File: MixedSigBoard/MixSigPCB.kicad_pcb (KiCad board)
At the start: 2 copper layers, 108 parts, among them J3 2x5 1.27mm, J4 USB_C_Receptacle_USB2.0, U1 REF3033AIDBZT, U10 HT7533-1, U11 MCP6001T-E/OT, U3 MCP6001T-E/OT, U4 MCP6001T-E/OT, U6 MCP6001T-E/OT, U7 STM32F103CBT6, U8 USBLC6-2SC6, U9 TLV62569DBV, Y1 16MHz

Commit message: -Renumber components to match sheet number -Created PCB Constraints and Set-up
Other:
- copper layers 2 -> 4
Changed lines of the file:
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@@
 	(generator_version "9.0")
 	(general
-		(thickness 1.6)
+		(thickness 1.591)
 		(legacy_teardrops no)
 	)
@@
 	(layers
 		(0 "F.Cu" signal)
+		(4 "In1.Cu" power)
+		(6 "In2.Cu" power)
 		(2 "B.Cu" signal)
 		(9 "F.Adhes" user "F.Adhesive")
@@
 	)
 	(setup
+		(stackup
+			(layer "F.SilkS"
+				(type "Top Silk Screen")
+			)
+			(layer "F.Paste"
+				(type "Top Solder Paste")
+			)
+			(layer "F.Mask"
+				(type "Top Solder Mask")
+				(thickness 0.01)
+			)
+			(layer "F.Cu"
+				(type "copper")
+				(thickness 0.035)
+			)
+			(layer "dielectric 1"
+				(type "prepreg")
+				(thickness 0.2)
+				(material "FR4")
+				(epsilon_r 4.6)
+				(loss_tangent 0.02)
+			)
+			(layer "In1.Cu"
+				(type "copper")
+				(thickness 0.018)
+			)
+			(layer "dielectric 2"
+				(type "core")
+				(thickness 1.065)
+				(material "FR4")
+				(epsilon_r 4.6)
+				(loss_tangent 0.02)
+			)
+			(layer "In2.Cu"
+				(type "copper")
+				(thickness 0.018)
+			)
+			(layer "dielectric 3"
+				(type "prepreg")
+				(thickness 0.2)
+				(material "FR4")
+				(epsilon_r 4.6)
+				(loss_tangent 0.02)
+			)
+			(layer "B.Cu"
+				(type "copper")
+				(thickness 0.035)
+			)
+			(layer "B.Mask"
+				(type "Bottom Solder Mask")
+				(thickness 0.01)
+			)
+			(layer "B.Paste"
+				(type "Bottom Solder Paste")
+			)
+			(layer "B.SilkS"
+				(type "Bottom Silk Screen")
+			)
+			(copper_finish "ENIG")
+			(dielectric_constraints no)
+		)
 		(pad_to_mask_clearance 0)
 		(allow_soldermask_bridges_in_footprints no)

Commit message: Add all footprints
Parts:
- added J1: 031-5640-1010, MixSig_Footprints_KiCad6:AMPHENOL-BNC-031-5640-1010, F.Cu at (191.1, 106.2)
- added J2: 031-5640-1010, MixSig_Footprints_KiCad6:AMPHENOL-BNC-031-5640-1010, F.Cu at (191.1, 124.7)
- added L2: CMF3216F-900-2P-T, MixSig_Footprints_KiCad6:CMC-1206, F.Cu at (207.7, 123.0)
- added L4: 68u, MixSig_Footprints_KiCad6:MWSA0603S, F.Cu at (210.3, 115.5)
- added U2: ADC141S626CIMM_NOPB, MixSig_Footprints_KiCad6:VSSOP-10, F.Cu at (201.3, 96.6)
- added U5: DAC7563SDGSR, MixSig_Footprints_KiCad6:VSSOP-10, F.Cu at (201.3, 115.1)
- renumbered C2 to C1, C11 to C10, C12 to C11, C13 to C12, C14 to C13, C15 to C14, C16 to C15, C17 to C16, C18 to C17, C19 to C18, C20 to C19, C3 to C2, C21 to C20, C22 to C21, C23 to C22, C24 to C23, C25 to C24, C26 to C25, C27 to C26, C28 to C27, C29 to C28, C30 to C29, C4 to C3, C31 to C30, C32 to C31, C33 to C32, C34 to C33, C35 to C34, C36 to C35, C37 to C36, C1 to C37, C45 to C38, C38 to C39, C5 to C4, C39 to C40, C40 to C41, C41 to C42, C42 to C43, C43 to C44, C44 to C45, C6 to C5, C7 to C6, C8 to C7, C9 to C8, C10 to C9, L2 to L1, L1 to L3, R2 to R1, R11 to R10, R12 to R11, R13 to R12, R14 to R13, R15 to R14, R16 to R15, R17 to R16, R18 to R17, R19 to R18, R20 to R19, R3 to R2, R21 to R20, R22 to R21, R23 to R22, R24 to R23, R25 to R24, R26 to R25, R27 to R26, R28 to R27, R29 to R28, R30 to R29, R4 to R3, R31 to R30, R1 to R31, R5 to R4, R6 to R5, R7 to R6, R8 to R7, R9 to R8, R10 to R9

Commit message: add pcb footprints
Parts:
- moved L2 76.8 mm to (141.2, 84.5)
- moved D3 40.0 mm to (171.5, 111.7)
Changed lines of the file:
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@@
 		)
 		(embedded_fonts no)
-		(model "C:/Users/phili/OneDrive/Electrical/STEP FILES/BNC-31-5640-1010.stp"
+		(model "${KICAD9_3DMODEL_DIR}/Connector_USB.3dshapes/31-5640-1010.stp"
 			(offset
 				(xyz 0 30.15 8)
@@
 		)
 		(embedded_fonts no)
-		(model "${KICAD9_3DMODEL_DIR}/Connector_USB.3dshapes/USB_C_Receptacle_HRO_TYPE-C-31-M-12.step"
+		(model "${KICAD9_3DMODEL_DIR}/Connector_USB.3dshapes/HRO_TYPE-C-31-M-12.step"
 			(offset
-				(xyz 0 0 0)
+				(xyz -4.45 -3.9 0)
 			)
 			(scale
@@
 			)
 			(rotate
-				(xyz 0 0 0)
+				(xyz -0 -0 -0)
 			)
 		)
@@
 	(footprint "MixSig_Footprints_KiCad6:CMC-1206"
 		(layer "F.Cu")
-		(at 207.675 122.95)
+		(at 141.175 84.45)
 		(property "Reference" "L2"
 			(at 0 -3 0)
@@
 		)
 		(embedded_fonts no)
-		(model "C:/Users/phili/OneDrive/Electrical/STEP FILES/CMC-1206.step"
+		(model "${KICAD9_3DMODEL_DIR}/LED_SMD.3dshapes/Coilcraft-1206CS.step"
 			(offset
 				(xyz 0 0 0)
@@
 		)
 		(embedded_fonts no)
-		(model "C:/Users/phili/OneDrive/Electrical/STEP FILES/MWSA0603S.STEP"
+		(model "${KICAD9_3DMODEL_DIR}/Connector_USB.3dshapes/IND_MWSA0603S_SNL.step"
 			(offset
 				(xyz 0 0 0)
@@
 	(footprint "LED_SMD:LED_Avago_PLCC4_3.2x2.8mm_CW"
 		(layer "F.Cu")
-		(at 131.57 114.31)
+		(at 171.5 111.695)
 		(descr "3.2mm x 2.8mm PLCC4 RGB LED, https://docs.broadcom.com/docs/AV02-4186EN")
 		(tags "LED Avago PLCC-4 3528 ASMB-MTB0-0A3A2")
@@
 		)
 		(embedded_fonts no)
-		(model "${KICAD9_3DMODEL_DIR}/LED_SMD.3dshapes/LED_Avago_PLCC4_3.2x2.8mm_CW.step"
+		(model "${KICAD9_3DMODEL_DIR}/LED_SMD.3dshapes/PLCC4.stp"
 			(offset
 				(xyz 0 0 0)
@@
 		)
 		(embedded_fonts no)
-		(model "C:/Users/phili/OneDrive/Electrical/STEP FILES/BNC-31-5640-1010.stp"
+		(model "${KICAD9_3DMODEL_DIR}/Connector_USB.3dshapes/31-5640-1010.stp"
 			(offset
 				(xyz 0 30.15 8)

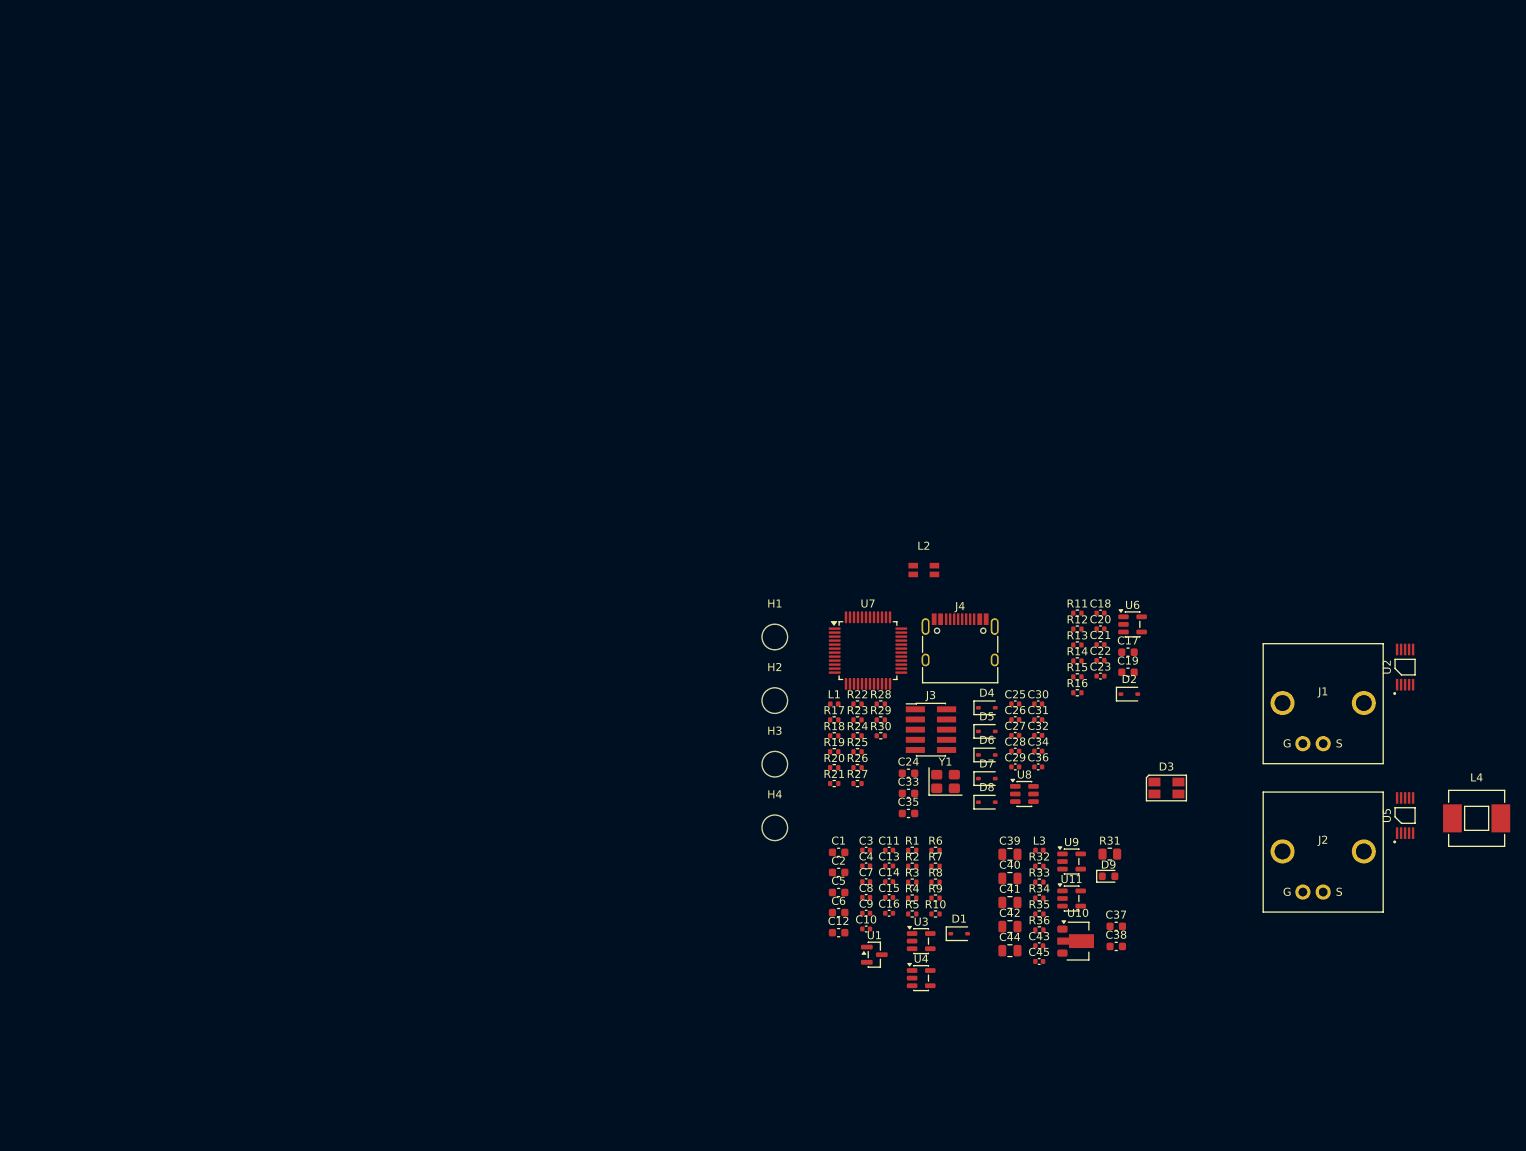
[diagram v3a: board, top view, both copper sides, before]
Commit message: Layout w/o Traces for MCU, ADC page
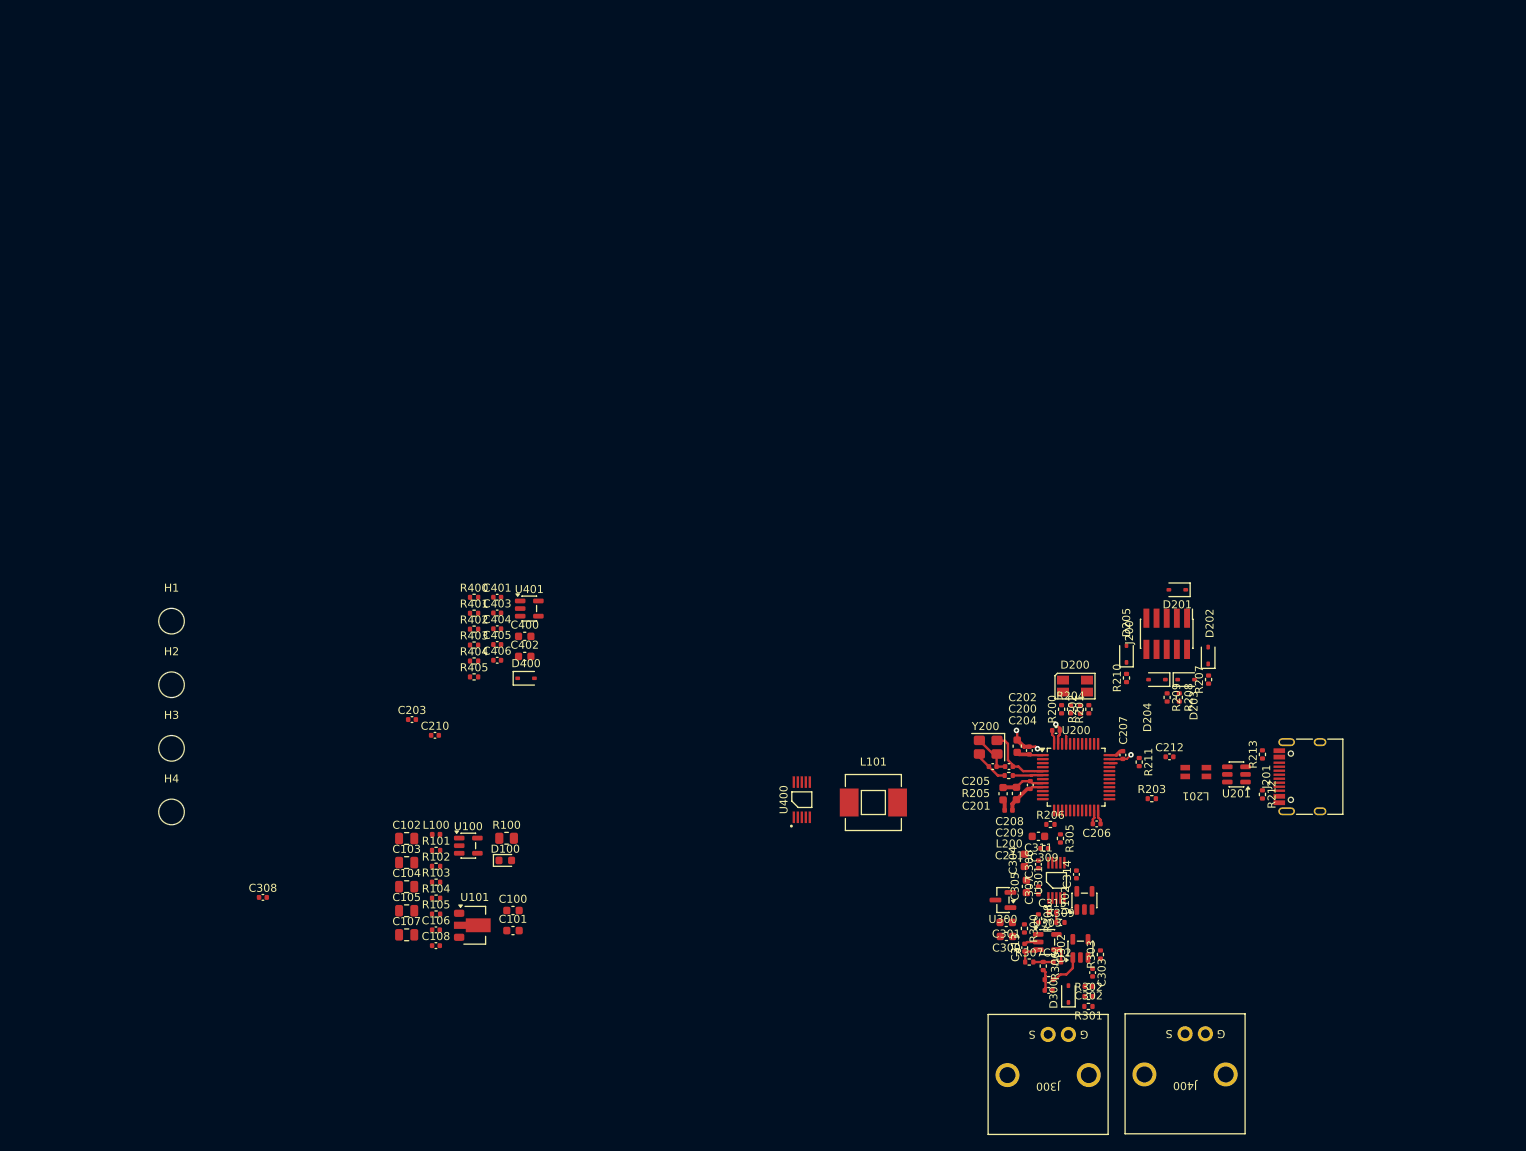
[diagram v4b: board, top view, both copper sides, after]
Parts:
- moved C102 75.4 mm to (76.5, 118.0)
- moved C103 75.4 mm to (76.5, 121.0)
- moved C104 75.4 mm to (76.5, 124.0)
- moved C105 75.4 mm to (76.5, 127.0)
- moved C107 75.4 mm to (76.5, 130.0)
- moved C308 75.4 mm to (58.6, 125.4)
- moved D400 75.4 mm to (91.5, 98.0)
- moved H1 75.4 mm to (47.1, 90.8)
- moved H2 75.4 mm to (47.1, 98.8)
- moved H3 75.4 mm to (47.1, 106.7)
- moved H4 75.4 mm to (47.1, 114.7)
- moved L100 75.4 mm to (80.2, 117.5)
- moved L101 75.4 mm to (134.9, 113.5)
- moved R100 75.4 mm to (89.0, 118.0)
- moved R101 75.4 mm to (80.2, 119.5)
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- renumbered C37 to C100, C38 to C101, C39 to C102, C40 to C103, C41 to C104, C42 to C105, C43 to C106, C44 to C107, C45 to C108, C24 to C200, C25 to C201, C26 to C202, C27 to C203, C28 to C204, C29 to C205, C30 to C206, C31 to C207, C32 to C208, C33 to C209, C34 to C210, C35 to C211, C36 to C212, C1 to C300, C2 to C301, C3 to C302, C4 to C303, C5 to C304, C6 to C305, C7 to C306, C8 to C307, C9 to C308, C10 to C309, C11 to C310, C12 to C311, C13 to C312, C14 to C313, C15 to C314, C16 to C315, C17 to C400, C18 to C401, C19 to C402, C20 to C403, C21 to C404, C22 to C405, C23 to C406, D9 to D100, D3 to D200, D4 to D201, D5 to D202, D6 to D203, D7 to D204, D8 to D205, D1 to D300, D2 to D400, J3 to J200, J4 to J201, J1 to J300, J2 to J400, L3 to L100, L4 to L101, L1 to L200, L2 to L201, R31 to R100, R32 to R101, R33 to R102, R34 to R103, R35 to R104, R36 to R105, R17 to R200, R18 to R201, R19 to R202, R20 to R203, R21 to R204, R22 to R205, R23 to R206, R24 to R207, R25 to R208, R26 to R209, R27 to R210, R28 to R211, R29 to R212, R30 to R213, R1 to R300, R2 to R301, R3 to R302, R4 to R303, R5 to R304, R6 to R305, R7 to R306, R8 to R307, R9 to R308, R10 to R309, R11 to R400, R12 to R401, R13 to R402, R14 to R403, R15 to R404, R16 to R405, U9 to U100, U10 to U101, U11 to U102, U7 to U200, U8 to U201, U1 to U300, U2 to U301, U3 to U302, U4 to U303, U5 to U400, U6 to U401, Y1 to Y200
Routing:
- net GND: track 0.00 -> 24.4 mm, vias 0 -> 4
- net +3V3: track 0.00 -> 9.86 mm
- net /MCU/HSE_IN: track 0.00 -> 9.44 mm
- net VDDA: track 0.00 -> 5.42 mm
- net /MCU/XTAL_IN: track 0.00 -> 4.51 mm
- net /ADC/IN_BUF_OUT: track 0.00 -> 4.41 mm
- net /MCU/HSE_OUT: track 0.00 -> 3.91 mm
- net /ADC/IN_AA_BUF_IN: track 0.00 -> 3.13 mm
- net Net-(C312-Pad1): track 0.00 -> 2.52 mm
- net Net-(C310-Pad1): track 0.00 -> 2.40 mm
- net /ADC/IN_AA_BUF_OUT: track 0.00 -> 2.15 mm
- net /ADC/ADC_IN-: track 0.00 -> 1.25 mm
- net /MCU/TIM4_CH3: track 0.00 -> 0.97 mm
- net /MCU/SWDIO: track 0.00 -> 0.91 mm

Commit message: Finished general PCB placement
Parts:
- moved D205 143.2 mm to (41.5, 24.9)
- moved D201 142.8 mm to (48.0, 17.6)
- moved D202 142.8 mm to (51.8, 25.9)
- moved D203 142.8 mm to (49.1, 28.9)
- moved D204 142.8 mm to (45.4, 28.9)
- moved J200 142.8 mm to (46.6, 23.1)
- moved R207 142.8 mm to (51.9, 28.9)
- moved R210 142.8 mm to (41.6, 28.7)
- moved R208 142.8 mm to (48.2, 31.1)
- moved R209 142.8 mm to (46.7, 31.1)
- moved R300 139.1 mm to (38.0, 52.2), turned to 90 degrees
- moved C300 138.3 mm to (38.7, 50.2), turned to 0 degrees
- moved C302 131.7 mm to (48.7, 69.0)
- moved C303 131.7 mm to (49.2, 67.3)
- moved C310 131.7 mm to (43.7, 69.5)
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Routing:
- net +3.3VA: track 0.00 -> 6.23 mm
- net GND: track 24.4 -> 28.9 mm
- net /DAC/OUT_AA_BUF_OUT: track 0.00 -> 3.81 mm
- net /DAC/OUT_AA_BUF_IN: track 0.00 -> 3.48 mm
- net Net-(C404-Pad1): track 0.00 -> 2.52 mm
- net /DAC/DAC_OUT_B: track 0.00 -> 2.50 mm
- net /DAC/DAC_OUT_A: track 0.00 -> 1.65 mm
- net Net-(C403-Pad1): track 0.00 -> 1.37 mm
- net /DAC/OUT: track 0.00 -> 1.04 mm
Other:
- board outline added: 58.3 x 75.8 mm
- board text added: "Analog"
- board text added: "Austin Adam"
- board text added: "Digital"

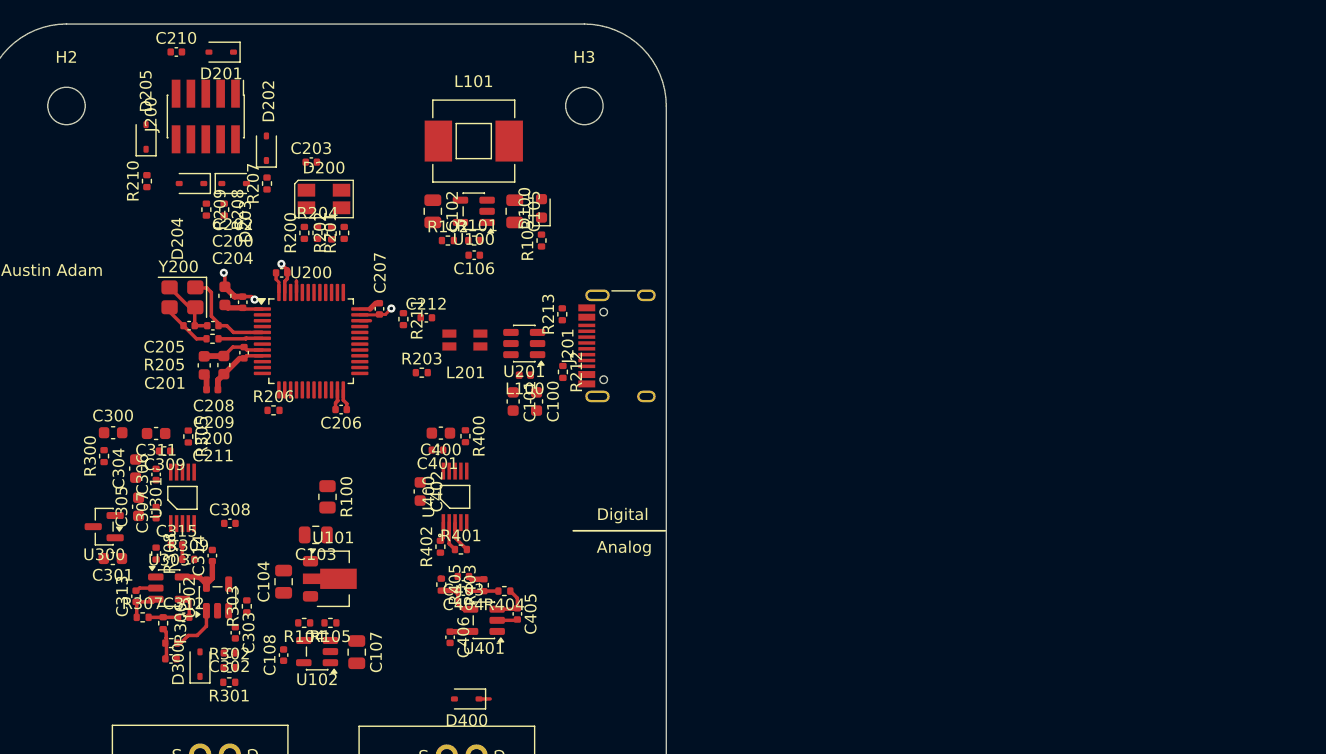
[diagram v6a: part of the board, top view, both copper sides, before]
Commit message: add routing to SWD,RGB LED's, USB, partial buck, partial power decoupling
- Copper pours to lower inductance/EMI/better return current
- Differential traces on USB, 50ohm single ended for SPI & for all signal lines for good practice
- Grounding via's near ground pin and slightly towards power side to minimize return path
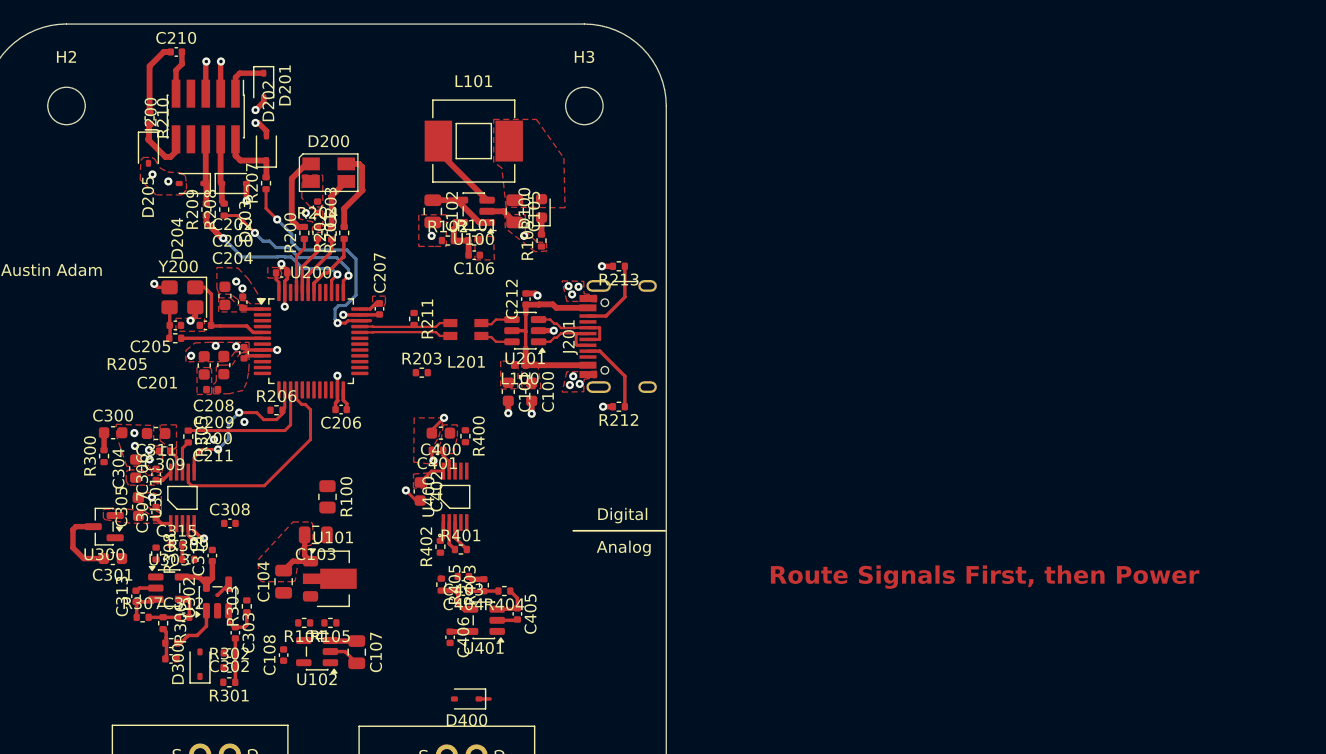
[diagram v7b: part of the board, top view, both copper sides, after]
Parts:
- moved C212 8.65 mm to (74.0, 38.8), turned to 90 degrees
- moved R213 6.34 mm to (82.0, 36.0), turned to 180 degrees
- moved R212 5.63 mm to (82.0, 48.0), turned to 180 degrees
- moved R210 5.38 mm to (41.9, 23.3), turned to -90 degrees
- moved D201 4.61 mm to (51.6, 20.5), turned to -90 degrees
- moved C203 3.89 mm to (56.2, 30.9), turned to -90 degrees
- moved R205 3.19 mm to (44.0, 42.1)
- moved D200 2.29 mm to (57.1, 27.9)
- moved D205 1.22 mm to (41.8, 26.1), turned to -90 degrees
- moved C205 1.18 mm to (44.0, 41.0)
- moved U201 1.10 mm to (74.0, 41.5)
- moved L100 0.95 mm to (73.5, 44.4)
- moved C100 0.92 mm to (74.5, 46.7)
- moved C101 0.92 mm to (72.5, 46.7)
- moved R211 0.91 mm to (64.5, 40.5)
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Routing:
- net GND: track 28.9 -> 67.3 mm, vias 4 -> 46
- net /MCU/SWDIO: track 0.91 -> 21.1 mm, vias 0 -> 2
- net SPI1_MISO: track 0.00 -> 18.0 mm
- net VBUS: track 0.00 -> 17.2 mm
- net /MCU/SWO: track 0.00 -> 15.5 mm, vias 0 -> 2
- net /MCU/SWCLK: track 0.00 -> 14.7 mm, vias 0 -> 2
- net SPI1_NSS: track 0.00 -> 13.7 mm, vias 0 -> 2
- net SPI1_SCK: track 0.00 -> 11.9 mm
- net /MCU/USB_D+: track 0.00 -> 7.95 mm
- net /MCU/USB_D-: track 0.00 -> 7.88 mm
- net /MCU/USB_CONN_D+: track 0.00 -> 7.52 mm
- net /MCU/USB_CONN_D-: track 0.00 -> 7.46 mm
- net /MCU/LED_G_K: track 0.00 -> 7.26 mm
- net +5V: track 0.00 -> 7.08 mm
- net /MCU/LED_R_K: track 0.00 -> 7.03 mm
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- added copper zone on F.Cu, net +3.3VA
- added copper zone on F.Cu, net +3V3
- added copper zone on F.Cu, net +5V
- added copper zone on F.Cu, net /ADC/ADC_VREF
- added copper zone on F.Cu, net /DAC/DAC_VREF
- added copper zone on F.Cu, net GND
- added copper zone on In1.Cu, net GND
- added copper zone on In2.Cu, net GND
- added copper zone on F.Cu, net VBUS
- added copper zone on F.Cu, net VDDA
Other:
- board text added: "Route Signals First, then Power"
